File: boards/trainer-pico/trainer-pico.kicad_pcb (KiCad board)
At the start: 2 copper layers, 132.1 x 99.1 mm, 31 parts, among them J1 Conn_01x08_Pin, J11 Conn_01x17_Pin, J12 Conn_01x17_Socket, J13 Conn_01x17_Socket, J14 Conn_01x17_Pin, J15 Barrel_Jack_Switch, J2 Conn_01x04_Pin, J3 Conn_01x06_Pin, J4 Conn_01x04_Pin, J5 Conn_01x04_Pin, J6 Conn_01x08_Socket, J7 Conn_01x04_Socket, U2 L7805, U3 L7809

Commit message: 配置修正
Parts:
- removed J6: Conn_01x08_Socket, Connector_PinSocket_2.54mm:PinSocket_1x08_P2.54mm_Vertical
- removed J7: Conn_01x04_Socket, Connector_PinSocket_2.54mm:PinSocket_1x04_P2.54mm_Vertical
- moved J1 2.54 mm to (129.5, 58.4)
- moved J2 2.54 mm to (157.5, 58.4)
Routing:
- net /GP_7: track 107.5 -> 98.8 mm
- net /GP_4: track 96.7 -> 88.0 mm
- net /GP_3: track 93.1 -> 84.4 mm
- net /GP_5: track 100.3 -> 91.6 mm
- net /GP_6: track 103.9 -> 95.2 mm
- net /GP_0: track 84.0 -> 75.3 mm
- net /GP_2: track 89.5 -> 81.5 mm
- net /GP_1: track 85.9 -> 78.9 mm
- net /ADC_2: track 90.7 -> 85.6 mm
- net /ADC_1: track 88.6 -> 83.6 mm
- net /ADC_3: track 92.6 -> 87.5 mm
- net /ADC_0: track 86.6 -> 81.6 mm
- net (no net): vias 1 -> 0
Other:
- outline, holes or cut-outs redrawn

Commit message: 回路の更新と、AW の修正
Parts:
- added J6: Conn_02x15_Odd_Even, Connector_PinSocket_2.54mm:PinSocket_2x15_P2.54mm_Horizontal, F.Cu at (132.1, 68.6)
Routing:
- net /UART_PICO_RX: track 49.3 -> 111.2 mm
- net /UART_PICO_TX: track 49.3 -> 110.9 mm
- net /I2C_SDA: track 60.4 -> 109.6 mm
- net /I2C_SCL: track 62.2 -> 111.1 mm
- net /SPI_CS: track 58.0 -> 104.3 mm
- net /SPI_MOSI: track 58.0 -> 104.0 mm
- net /SPI_SCK: track 58.0 -> 101.0 mm
- net /SPI_MISO: track 59.0 -> 101.9 mm
- net /GP_0: track 75.3 -> 97.1 mm
- net /GP_2: track 81.5 -> 100.0 mm
- net /ADC_2: track 85.6 -> 104.0 mm
- net /GP_4: track 88.0 -> 104.6 mm
- net /ADC_3: track 87.5 -> 104.1 mm
- net /GP_1: track 78.9 -> 94.8 mm
- net /ADC_0: track 81.6 -> 97.4 mm
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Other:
- outline, holes or cut-outs redrawn

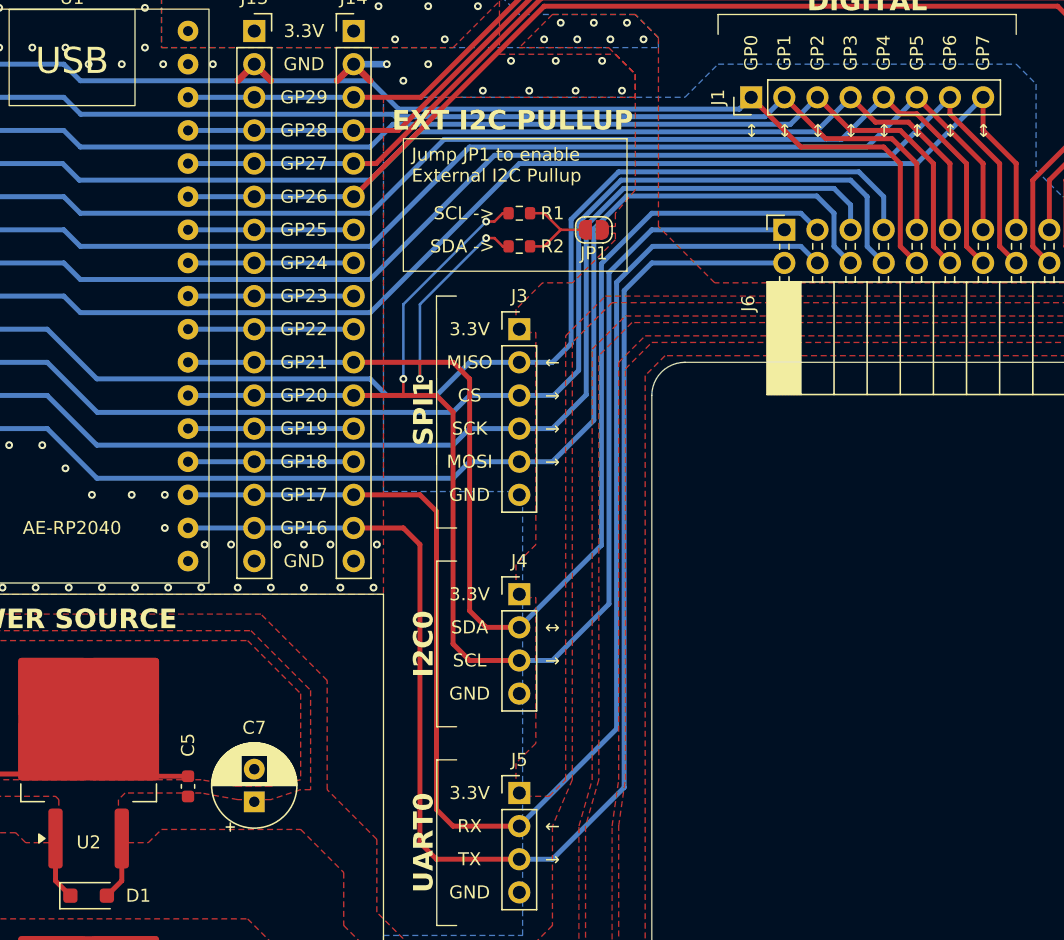
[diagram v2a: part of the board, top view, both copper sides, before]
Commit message: 配線修正
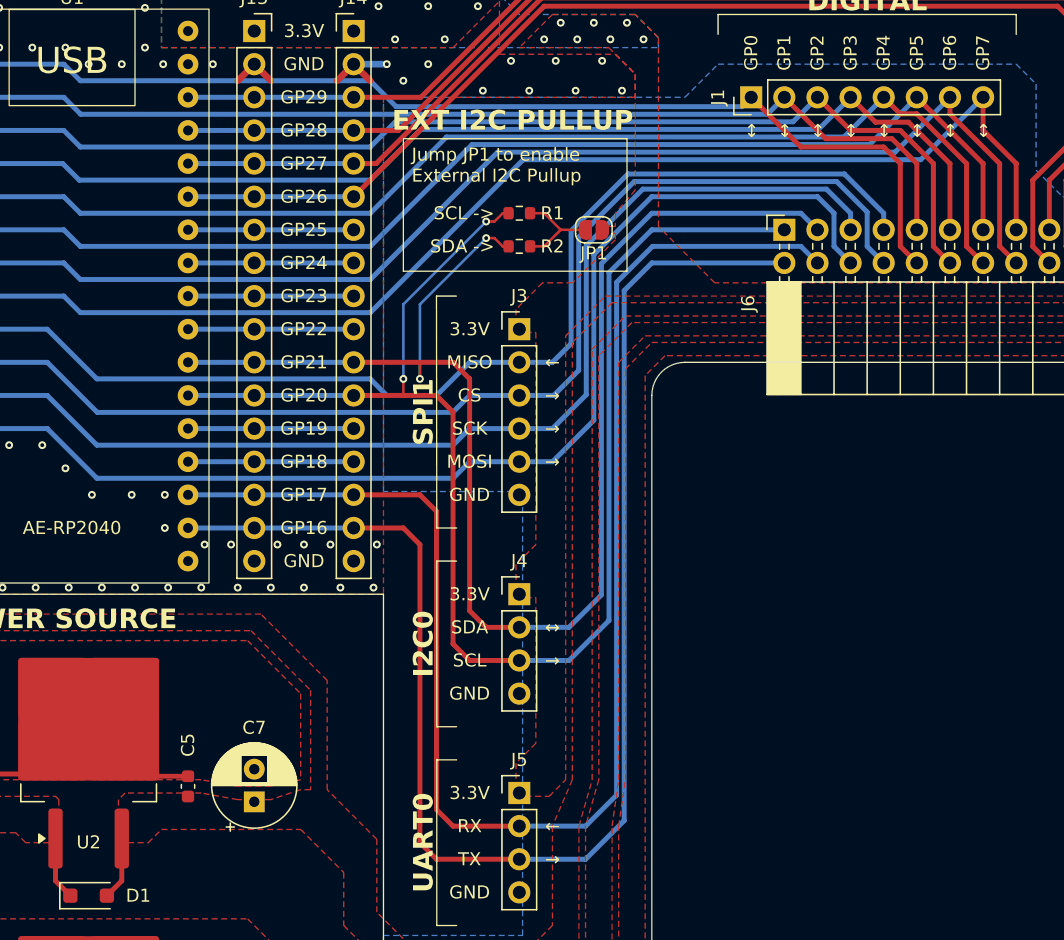
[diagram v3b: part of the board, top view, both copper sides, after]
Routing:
- net /UART_PICO_RX: track 111.2 -> 114.1 mm
- net /I2C_SDA: track 109.6 -> 111.8 mm
- net /UART_PICO_TX: track 110.9 -> 112.4 mm
- net /SPI_CS: track 104.3 -> 102.9 mm
- net /SPI_MISO: track 101.9 -> 100.5 mm
- net /SPI_SCK: track 101.0 -> 99.7 mm
- net /SPI_MOSI: track 104.0 -> 102.8 mm
- net /I2C_SCL: track 111.1 -> 111.8 mm

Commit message: 刻印変更
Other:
- board text added: "https://github.com/MOS-Elecs/trainer"
- board text removed: "https://github.com/53175ddd/trainer"
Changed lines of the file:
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@@
 		(layer "Edge.Cuts")
 	)
-	(gr_text "https://github.com/53175ddd/trainer"
+	(gr_text "https://github.com/MOS-Elecs/trainer"
 		(at 99.06 144.78 0)
 		(layer "B.SilkS")

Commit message: ピン番号を書いてみた
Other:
- board text added: "①"
- board text added: "②"
- board text added: "③"
- board text added: "④"
- board text added: "⑤"
- board text added: "⑥"
- board text added: "⑦"
- board text added: "⑧"
- board text added: "⑨"
- board text added: "⑩"
- board text added: "⑪"
- board text added: "⑫"
- board text added: "⑬"
- board text added: "⑭"
- board text added: "⑮"
- board text added: "⑯"
- board text added: "⑰"
- board text added: "⑱"
- board text added: "⑲"
- board text added: "⑳"
- board text added: "㉑"
- board text added: "㉒"
- board text added: "㉓"
- board text added: "㉔"
- board text added: "㉕"
- board text added: "㉖"
- board text added: "㉗"
- board text added: "㉘"
- board text added: "㉙"
- board text added: "㉚"

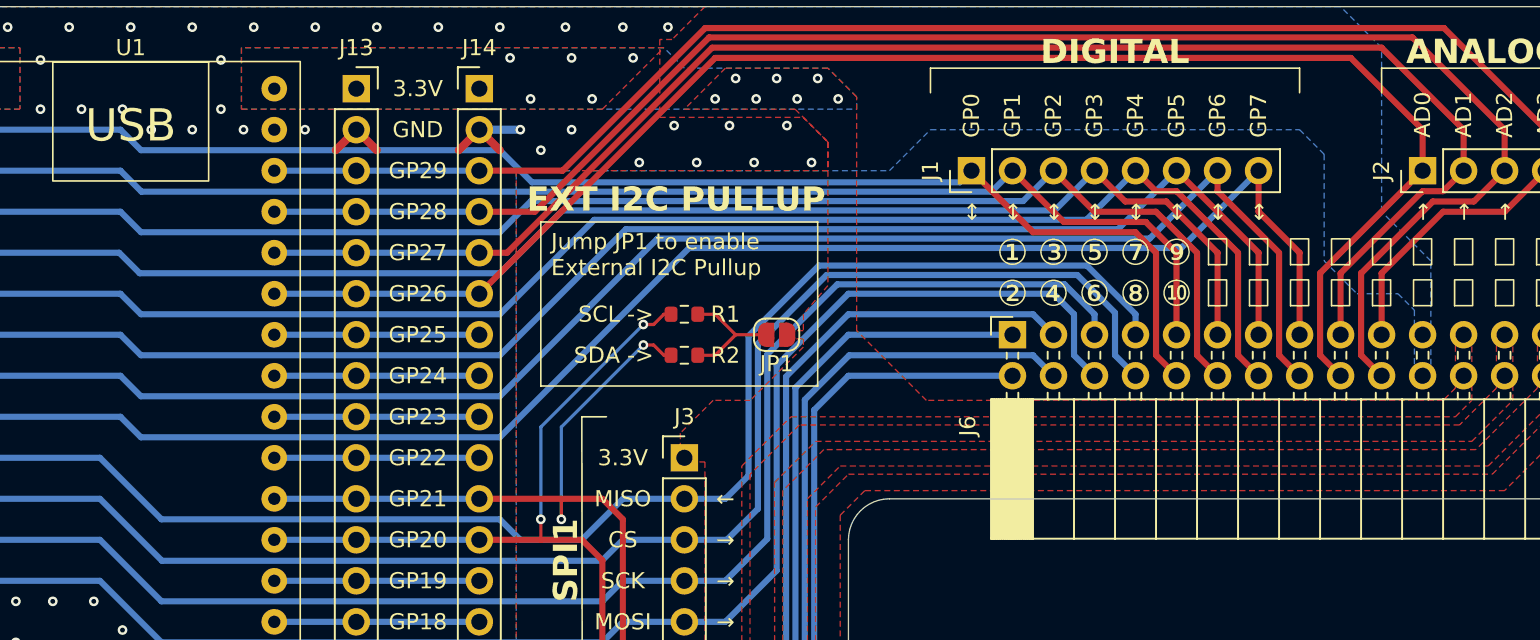
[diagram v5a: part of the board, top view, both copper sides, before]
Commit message: I2C プルアップの回路の配置を修正
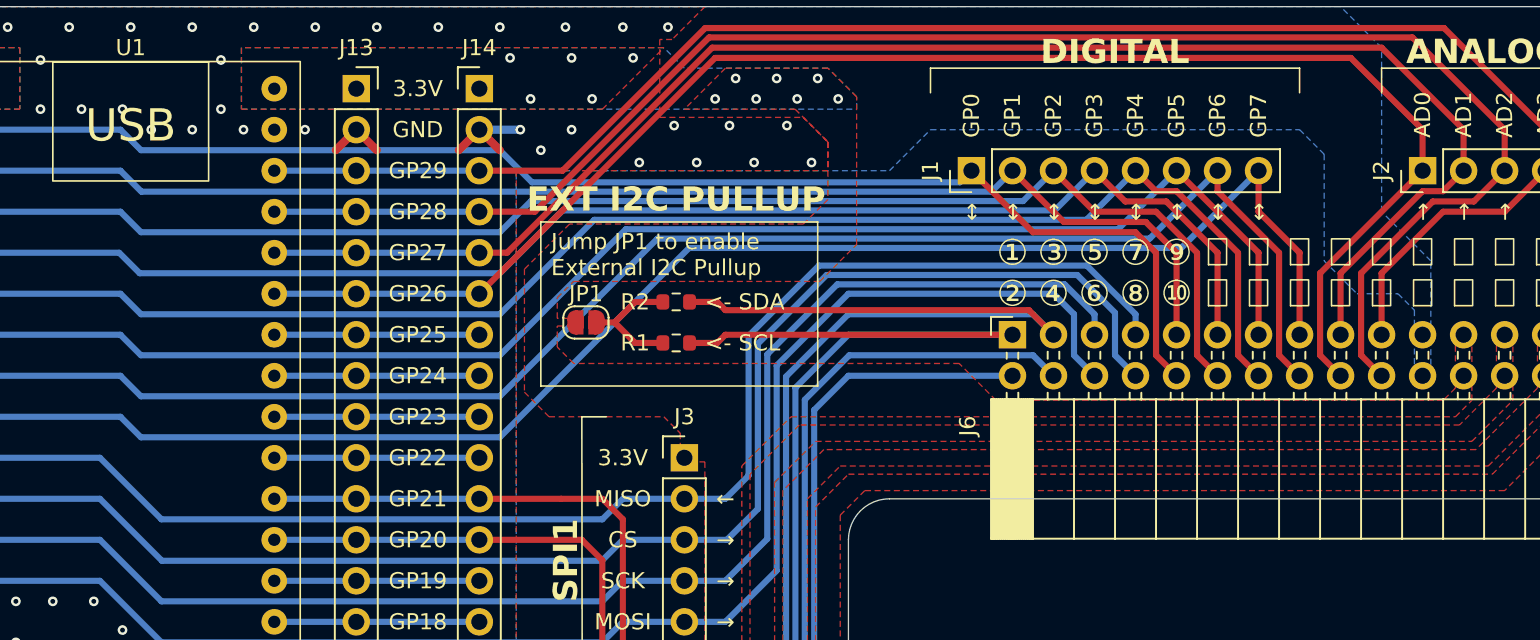
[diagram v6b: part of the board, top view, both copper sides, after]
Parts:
- moved JP1 11.8 mm to (105.7, 67.8), turned to 0 degrees
- moved R2 3.34 mm to (111.3, 66.5), turned to 0 degrees
- moved R1 1.85 mm to (111.3, 69.1), turned to 0 degrees
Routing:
- net /I2C_SDA: track 111.8 -> 119.0 mm, vias 2 -> 0
- net /I2C_SCL: track 111.8 -> 114.1 mm, vias 2 -> 0
- net /SPI_MISO: track 100.5 -> 99.5 mm
- net Net-(JP1-B): track 7.64 -> 8.15 mm
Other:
- board text added: "<- SCL"
- board text added: "<- SDA"
- board text removed: "SCL ->"
- board text removed: "SDA ->"

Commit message: light fix
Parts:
- moved R1 5.59 mm to (116.8, 69.1)
- moved R2 5.59 mm to (116.8, 66.5)
- moved JP1 5.59 mm to (111.3, 67.8)
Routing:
- net /I2C_SDA: track 119.0 -> 113.4 mm
- net /I2C_SCL: track 114.1 -> 108.5 mm
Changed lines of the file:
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@@
 	(footprint "Resistor_SMD:R_0603_1608Metric"
 		(layer "F.Cu")
-		(at 111.252 69.088)
+		(at 116.84 69.088)
 		(descr "Resistor SMD 0603 (1608 Metric), square (rectangular) end terminal, IPC_7351 nominal, (Body size source: IPC-SM-782 page 72, https://www.pcb-3d.com/wordpress/wp-content/uploads/ipc-sm-782a_amendment_1_and_2.pdf), generated with kicad-footprint-generator")
 		(tags "resistor")
 		(property "Reference" "R1"
-			(at -2.54 0 360)
+			(at -2.54 0 0)
 			(layer "F.SilkS")
 			(effects
@@
 		)
 		(property "Value" "R"
-			(at 0 1.43 360)
+			(at 0 1.43 0)
 			(layer "F.Fab")
 			(effects
@@
 		)
 		(fp_text user "${REFERENCE}"
-			(at 0 0 360)
+			(at 0 0 0)
 			(layer "F.Fab")
 			(effects
@@
 	(footprint "Jumper:SolderJumper-2_P1.3mm_Open_RoundedPad1.0x1.5mm"
 		(layer "F.Cu")
-		(at 105.664 67.818)
+		(at 111.252 67.818)
 		(descr "SMD Solder Jumper, 1x1.5mm, rounded Pads, 0.3mm gap, open")
 		(tags "solder jumper open")
 		(property "Reference" "JP1"
-			(at 0 -1.778 360)
+			(at 0 -1.778 0)
 			(layer "F.SilkS")
 			(effects
@@
 		)
 		(property "Value" "Jumper_2_Open"
-			(at 0 1.9 360)
+			(at 0 1.9 0)
 			(layer "F.Fab")
 			(effects
@@
 	(footprint "Resistor_SMD:R_0603_1608Metric"
 		(layer "F.Cu")
-		(at 111.252 66.548)
+		(at 116.84 66.548)
 		(descr "Resistor SMD 0603 (1608 Metric), square (rectangular) end terminal, IPC_7351 nominal, (Body size source: IPC-SM-782 page 72, https://www.pcb-3d.com/wordpress/wp-content/uploads/ipc-sm-782a_amendment_1_and_2.pdf), generated with kicad-footprint-generator")
 		(tags "resistor")
 		(property "Reference" "R2"
-			(at -2.54 0 360)
+			(at -2.54 0 0)
 			(layer "F.SilkS")
 			(effects
@@
 		)
 		(property "Value" "R"
-			(at 0 1.43 360)
+			(at 0 1.43 0)
 			(layer "F.Fab")
 			(effects
@@
 		)
 		(fp_text user "${REFERENCE}"
-			(at 0 0 360)
+			(at 0 0 0)
 			(layer "F.Fab")
 			(effects
@@
 	)
 	(gr_rect
-		(start 102.87 61.595)
-		(end 120.015 71.755)
+		(start 108.458 61.595)
+		(end 125.603 71.755)
 		(stroke
 			(width 0.1)
@@
 	)
 	(gr_text "EXT I2C PULLUP"
-		(at 111.252 60.198 0)
+		(at 116.84 60.198 0)
 		(layer "F.SilkS" knockout)
 		(effects
@@
 	)
 	(gr_text "<- SCL"
-		(at 113.03 69.088 0)
+		(at 118.618 69.088 0)
 		(layer "F.SilkS")
 		(effects
@@
 	)
 	(gr_text "<- SDA"
-		(at 113.03 66.548 0)
+		(at 118.618 66.548 0)
 		(layer "F.SilkS")
 		(effects
@@
 	)
 	(gr_text "Jump JP1 to enable\nExternal I2C Pullup"
-		(at 103.505 62.23 0)
+		(at 109.093 62.23 0)
 		(layer "F.SilkS")
 		(effects
@@
 	)
 	(segment
+		(start 119.888 68.58)
+		(end 132.08 68.58)
+		(width 0.381)
+		(layer "F.Cu")
+		(net 18)
+	)
+	(segment
 		(start 106.68 82.55)
 		(end 106.68 100.33)
@@
 	)
 	(segment
-		(start 113.792 69.088)
-		(end 114.3 68.58)
-		(width 0.381)
-		(layer "F.Cu")
-		(net 18)
-	)
-	(segment
-		(start 114.3 68.58)
-		(end 132.08 68.58)
+		(start 119.38 69.088)
+		(end 119.888 68.58)
 		(width 0.381)
 		(layer "F.Cu")
@@
 	)
 	(segment
-		(start 112.077 69.088)
-		(end 113.792 69.088)
+		(start 117.665 69.088)
+		(end 119.38 69.088)
 		(width 0.381)
 		(layer "F.Cu")
@@
 	)
 	(segment
-		(start 113.792 66.548)
-		(end 114.3 67.056)
+		(start 119.38 66.548)
+		(end 119.888 67.056)
+		(width 0.381)
+		(layer "F.Cu")
+		(net 19)
+	)
+	(segment
+		(start 133.096 67.056)
+		(end 119.888 67.056)
 		(width 0.381)
 		(layer "F.Cu")
@@
 	)
 	(segment
-		(start 112.077 66.548)
-		(end 113.792 66.548)
+		(start 117.665 66.548)
+		(end 119.38 66.548)
 		(width 0.381)
 		(layer "F.Cu")
@@
 	)
 	(segment
-		(start 114.3 67.056)
-		(end 133.096 67.056)
-		(width 0.381)
-		(layer "F.Cu")
-		(net 19)
-	)
-	(segment
 		(start 109.22 99.06)
 		(end 111.76 99.06)
@@
 	)
 	(segment
-		(start 110.427 69.088)
-		(end 108.712 69.088)
+		(start 116.015 69.088)
+		(end 114.3 69.088)
 		(width 0.381)
 		(layer "F.Cu")
@@
 	)
 	(segment
-		(start 108.712 66.548)
-		(end 110.427 66.548)
+		(start 114.3 66.548)
+		(end 116.015 66.548)
 		(width 0.381)
 		(layer "F.Cu")
@@
 	)
 	(segment
-		(start 107.442 67.818)
-		(end 108.712 66.548)
+		(start 113.03 67.818)
+		(end 114.3 66.548)
 		(width 0.381)
 		(layer "F.Cu")
@@
 	)
 	(segment
-		(start 108.712 69.088)
-		(end 107.442 67.818)
+		(start 114.3 69.088)
+		(end 113.03 67.818)
 		(width 0.381)
 		(layer "F.Cu")
@@
 	)
 	(segment
-		(start 106.314 67.818)
-		(end 107.442 67.818)
+		(start 111.902 67.818)
+		(end 113.03 67.818)
 		(width 0.381)
 		(layer "F.Cu")
@@
 		(polygon
 			(pts
-				(xy 101.854 64.516) (xy 101.854 72.136) (xy 103.378 73.66) (xy 110.49 73.66) (xy 111.506 74.676)
-				(xy 111.506 76.454) (xy 113.03 76.454) (xy 113.03 92.71) (xy 111.506 94.234) (xy 111.506 96.774)
-				(xy 113.03 96.774) (xy 113.03 107.95) (xy 111.506 109.474) (xy 111.506 112.014) (xy 114.046 112.014)
-				(xy 115.316 110.744) (xy 115.316 76.708) (xy 118.364 73.66) (xy 159.512 73.66) (xy 160.528 72.644)
-				(xy 160.528 68.072) (xy 159.512 68.072) (xy 159.512 71.882) (xy 158.75 72.644) (xy 131.064 72.644)
-				(xy 128.778 70.358) (xy 104.902 70.358) (xy 103.886 69.342) (xy 103.886 68.039025) (xy 105.156 68.039025)
-				(xy 105.156 67.564) (xy 103.886 67.564) (xy 103.886 66.294) (xy 104.902 65.278) (xy 120.142 65.278)
-				(xy 122.428 62.992) (xy 122.428 53.848) (xy 120.65 52.07) (xy 114.3 52.07) (xy 111.76 54.61) (xy 118.618 54.61)
-				(xy 120.65 56.642) (xy 120.65 60.198) (xy 119.126 61.722) (xy 104.648 61.722)
+				(xy 106.68 63.246) (xy 106.68 72.136) (xy 108.204 73.66) (xy 110.49 73.66) (xy 111.506 74.676) (xy 111.506 76.454)
+				(xy 113.03 76.454) (xy 113.03 92.71) (xy 111.506 94.234) (xy 111.506 96.774) (xy 113.03 96.774)
+				(xy 113.03 107.95) (xy 111.506 109.474) (xy 111.506 112.014) (xy 114.046 112.014) (xy 115.316 110.744)
+				(xy 115.316 76.708) (xy 118.364 73.66) (xy 159.512 73.66) (xy 160.528 72.644) (xy 160.528 68.072)
+				(xy 159.512 68.072) (xy 159.512 71.882) (xy 158.75 72.644) (xy 131.064 72.644) (xy 128.778 70.358)
+				(xy 110.49 70.358) (xy 109.474 69.342) (xy 109.474 68.072) (xy 110.744 68.072) (xy 110.744 67.564)
+				(xy 109.474 67.564) (xy 109.474 66.294) (xy 110.49 65.278) (xy 121.92 65.278) (xy 123.19 64.008)
+				(xy 123.19 54.61) (xy 120.65 52.07) (xy 114.3 52.07) (xy 111.76 54.61) (xy 118.618 54.61) (xy 120.65 56.642)
+				(xy 120.65 60.198) (xy 119.126 61.722) (xy 108.204 61.722)
 			)
 		)

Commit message: light AW fix
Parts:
- moved R1 0.51 mm to (116.8, 69.6)
- moved JP1 0.51 mm to (111.3, 68.3)
- moved R2 0.51 mm to (116.8, 67.1)
